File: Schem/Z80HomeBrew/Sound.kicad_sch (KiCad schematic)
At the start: 19 parts, among them J13 Conn_01x03, J6 STX-3120-3B, U18 SN76489AN, U19 SN76489AN, U20 LM386MX-1/NOPB, U4 SN74HC00ANSR

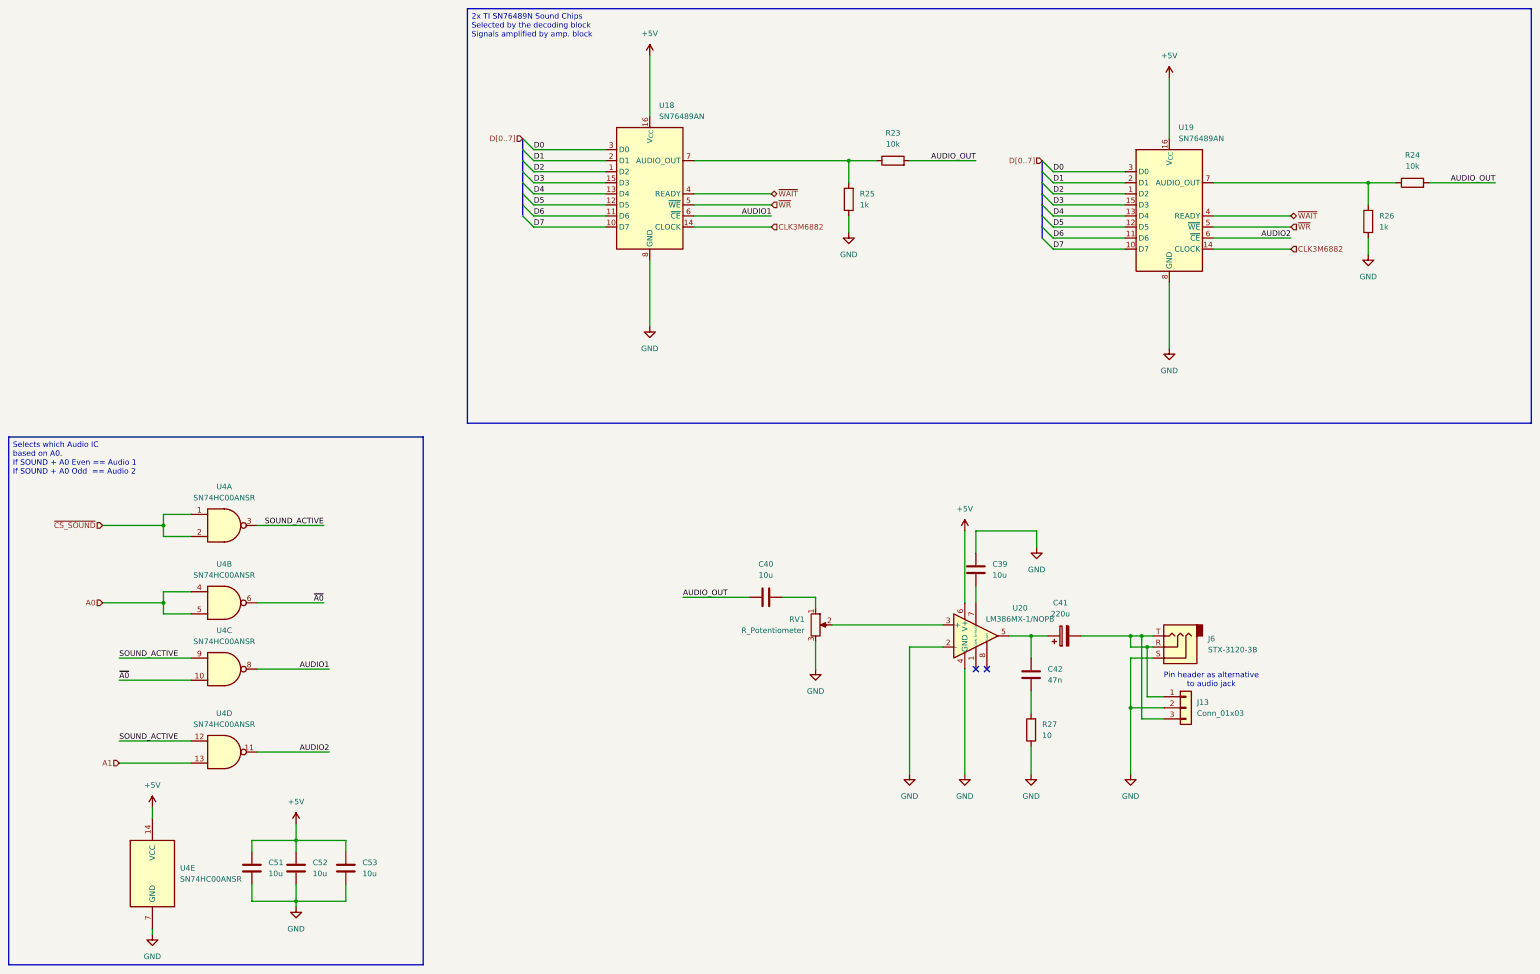
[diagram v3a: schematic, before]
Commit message: Added pBITzBackplane and MezzanineConnector
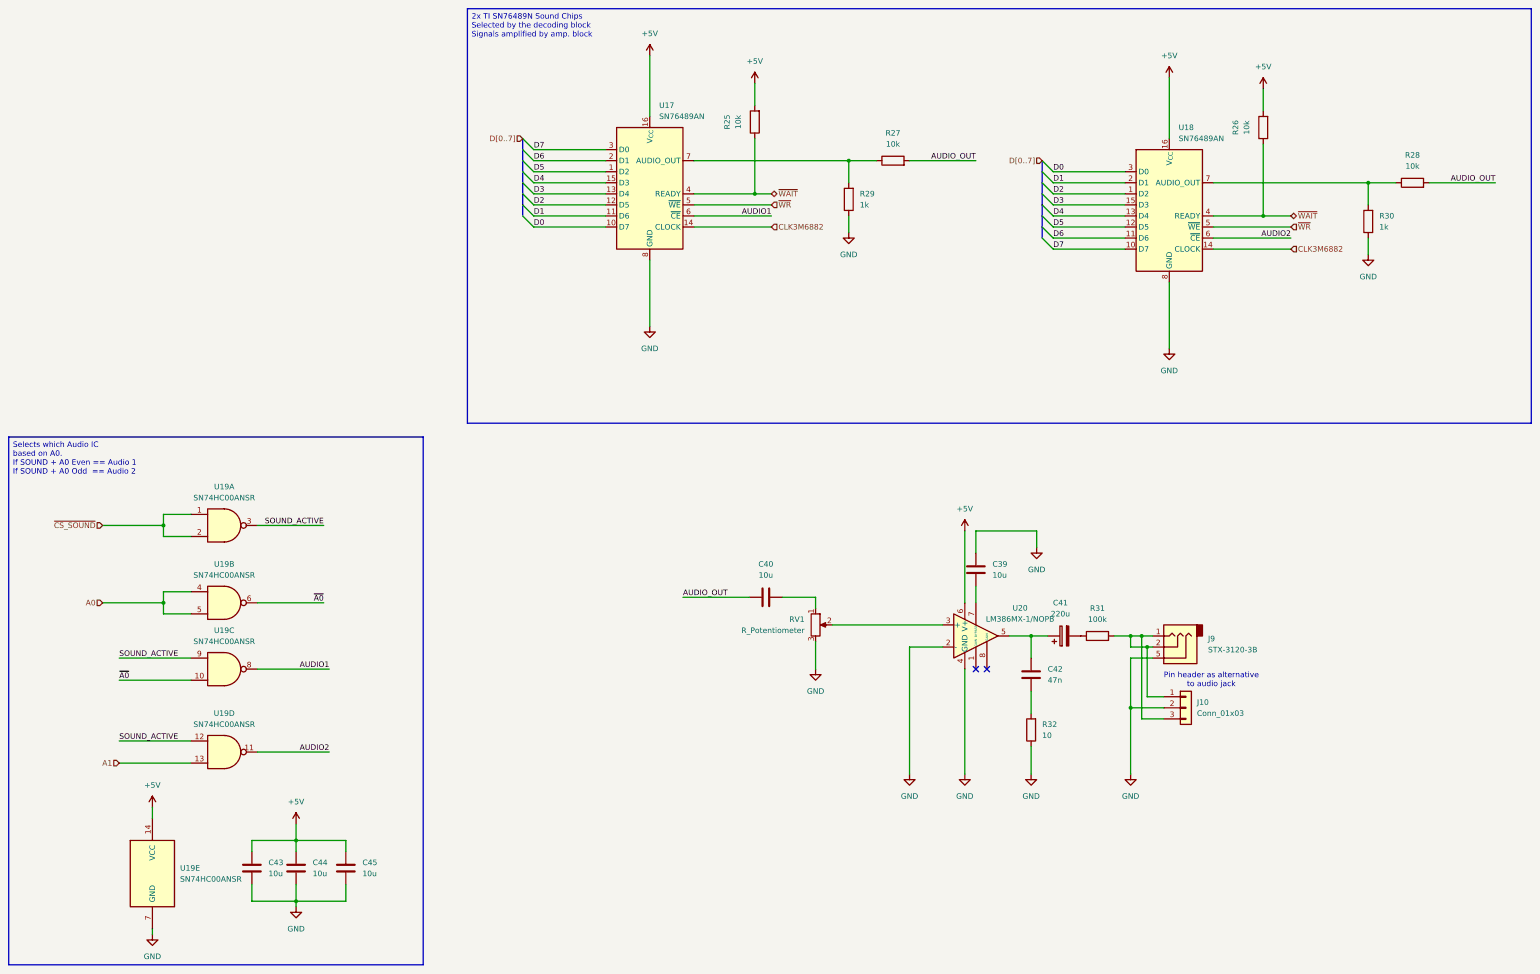
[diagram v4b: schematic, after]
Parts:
- added R25, R26: 10k, Resistor_SMD:R_0603_1608Metric, symbol Device:R
- added R31: 100k, Resistor_SMD:R_0603_1608Metric, symbol Device:R
- C39, C40: footprint Capacitor_SMD:C_1206_3216Metric -> Capacitor_SMD:C_0603_1608Metric; MANUFACTURER_PART_NUMBER (none) -> CL10X106MO8NRNC
- C41: footprint Capacitor_Tantalum_SMD:CP_EIA-3528-21_Kemet-B -> Capacitor_THT:CP_Radial_D6.3mm_P2.50mm; MANUFACTURER_PART_NUMBER (none) -> 16ZLH220MEFCT16.3X11
- C42: footprint Capacitor_SMD:C_1206_3216Metric -> Capacitor_SMD:C_0603_1608Metric; MANUFACTURER_PART_NUMBER (none) -> CL10B473KO8NNNC
- C43: renamed from C51; footprint Capacitor_SMD:C_1206_3216Metric -> Capacitor_SMD:C_0603_1608Metric; MANUFACTURER_PART_NUMBER (none) -> CL10X106MO8NRNC
- C44: renamed from C52; footprint Capacitor_SMD:C_1206_3216Metric -> Capacitor_SMD:C_0603_1608Metric; MANUFACTURER_PART_NUMBER (none) -> CL10X106MO8NRNC
- C45: renamed from C53; footprint Capacitor_SMD:C_1206_3216Metric -> Capacitor_SMD:C_0603_1608Metric; MANUFACTURER_PART_NUMBER (none) -> CL10X106MO8NRNC
- J10: renamed from J13; MANUFACTURER_PART_NUMBER (none) -> 732-5301-ND
- J9: renamed from J6; MANUFACTURER_PART_NUMBER (none) -> STX-3120-3B
- R27: renamed from R23; MANUFACTURER_PART_NUMBER (none) -> RC0603FR-0710KL
- R28: renamed from R24; MANUFACTURER_PART_NUMBER (none) -> RC0603FR-0710KL
- R29: renamed from R25; MANUFACTURER_PART_NUMBER (none) -> RMCF0603FT1K00
- R30: renamed from R26; MANUFACTURER_PART_NUMBER (none) -> RMCF0603FT1K00
- R32: renamed from R27; MANUFACTURER_PART_NUMBER (none) -> RMCF0603FT10R0
- RV1: MANUFACTURER_PART_NUMBER (none) -> 3266W-1-103LF
- U17: renamed from U18; MANUFACTURER_PART_NUMBER (none) -> 1-2199298-4
- U18: renamed from U19; MANUFACTURER_PART_NUMBER (none) -> 1-2199298-4
- U19: renamed from U4; MANUFACTURER_PART_NUMBER (none) -> SN74HC00ANSR
- U20: MANUFACTURER_PART_NUMBER (none) -> LM386MX-1/NOPB
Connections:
- net +5V: now also R25.2, R26.2
- net D0: now also U17.10 (D7); no longer U17.3 (D0)
- net D1: now also U17.11 (D6); no longer U17.2 (D1)
- net D2: now also U17.12 (D5); no longer U17.1 (D2)
- net D3: now also U17.13 (D4); no longer U17.15 (D3)
- net D4: now also U17.15 (D3); no longer U17.13 (D4)
- net D5: now also U17.1 (D2); no longer U17.12 (D5)
- net D6: now also U17.2 (D1); no longer U17.11 (D6)
- net D7: now also U17.3 (D0); no longer U17.10 (D7)
- net GND: now also J9.5; no longer J9.S
- net ~{WAIT}: now also R25.1, R26.1
- new net: J10.1 (Pin_1), J10.3 (Pin_3), J9.1, J9.2, R31.2
- new net: C41.2, R31.1
